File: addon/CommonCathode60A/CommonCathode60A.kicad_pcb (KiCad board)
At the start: 2 copper layers, 19 parts, among them J101 Conn_02x20_Odd_Even Header, J102 TBL008V-1000-08BE, J103 TBL008V-1000-08BE, K101 EW60-1A3-CL12D04, K102 EW60-1A3-CL12D04, K103 EW60-1A3-CL12D04, K104 EW60-1A3-CL12D04, K105 EW60-1A3-CL12D04, K106 EW60-1A3-CL12D04, K107 EW60-1A3-CL12D04, K108 EW60-1A3-CL12D04

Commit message: Better 60a board
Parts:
- moved H102 158.8 mm to (54.0, 133.0)
- moved H101 127.7 mm to (54.0, 27.0)
- moved J103 115.6 mm to (181.0, 125.0), turned to 90 degrees
- moved K101 90.3 mm to (154.0, 54.0), turned to 180 degrees
- moved K103 90.1 mm to (154.0, 74.0), turned to 180 degrees
- moved K107 82.9 mm to (154.0, 114.0), turned to 180 degrees
- moved K104 80.7 mm to (99.0, 74.0)
- moved K106 74.6 mm to (99.0, 94.0)
- moved H103 72.3 mm to (199.0, 27.0)
- moved J102 67.6 mm to (59.0, 125.0), turned to 90 degrees
- moved K102 67.3 mm to (99.0, 54.0)
- moved H104 50.2 mm to (199.0, 133.0)
- moved K108 34.5 mm to (99.0, 114.0)
- moved K105 28.4 mm to (154.0, 94.0), turned to 180 degrees
- moved J101 13.1 mm to (153.3, 40.1), turned to 270 degrees
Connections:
- net /K2_COIL_ON renamed /K4_COIL_ON
- J101 pad 13: /K2_COIL_OFF -> /K4_COIL_OFF
- J101 pad 14: /K2_COIL_OFF -> /K4_COIL_OFF
- K104 pad A2: /K2_COIL_OFF -> /K4_COIL_OFF
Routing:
- net /K3_OUT: track 0.00 -> 105.7 mm
- net /K1_OUT: track 0.00 -> 104.8 mm
- net /K2_OUT: track 0.00 -> 104.4 mm
- net /K4_OUT: track 0.00 -> 104.4 mm
- net /K8_IN: track 0.00 -> 103.0 mm
- net /K7_IN: track 0.00 -> 103.0 mm
- net /K6_IN: track 0.00 -> 103.0 mm
- net /K5_IN: track 0.00 -> 103.0 mm
- net /K5_OUT: track 0.00 -> 39.3 mm
- net /K8_OUT: track 0.00 -> 39.3 mm
- net /K7_OUT: track 0.00 -> 39.3 mm
- net /K6_OUT: track 0.00 -> 39.3 mm
- net /K1_IN: track 0.00 -> 36.9 mm
- net /K4_IN: track 0.00 -> 36.9 mm
- net /K3_IN: track 0.00 -> 36.9 mm
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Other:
- board outline added: 153 x 114 mm
- net class 30A Up to 230V AC added: clearance 1.25, trace_width 4, via_dia 9, via_drill 7
- net class 60A Up to 230V AC added: clearance 1.25, trace_width 8, via_dia 9, via_drill 7
- net class Default: clearance 0.2 -> 0.25; via_drill 0.4 -> 0.5
- rule trace_clearance: 0.2 -> 0.25

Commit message: Fix green
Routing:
- net /K5_OUT: track 39.3 -> 92.8 mm
- net /K8_OUT: track 39.3 -> 92.8 mm
- net /K7_OUT: track 39.3 -> 92.8 mm
- net /K6_OUT: track 39.3 -> 92.8 mm
- net /K4_IN: track 36.9 -> 88.7 mm
- net /K3_IN: track 36.9 -> 88.7 mm
- net /K2_IN: track 36.9 -> 88.7 mm
- net /K1_IN: track 36.9 -> 88.7 mm
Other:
- net class Default: clearance 0.25 -> 0.5; trace_width 0.25 -> 0.5
- rule trace_clearance: 0.25 -> 0.5

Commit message: Fix 60 Relay board
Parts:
- removed G101: LOGO_RUGLUDALLUR, BoatControl:Rugludallur-Logo_SilkScreen
- G102, LOGO102: moved to B.Cu
- LOGO101: footprint Symbol:KiCad-Logo2_20mm_SilkScreen -> Symbol:KiCad-Logo2_12mm_SilkScreen; moved to B.Cu
- moved LOGO101 391.9 mm to (73.0, 32.0)
- moved G102 324.8 mm to (125.5, 58.5)
- moved LOGO102 319.7 mm to (183.0, 33.5)
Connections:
- J101 pad 1: /K5_COIL_OFF -> /K1_COIL_ON
- J101 pad 10: /K6_COIL_OFF -> /K3_COIL_ON
- J101 pad 11: /K6_COIL_ON -> /K3_COIL_OFF
- J101 pad 12: /K6_COIL_ON -> /K3_COIL_OFF
- J101 pad 13: /K4_COIL_OFF -> /K4_COIL_ON
- J101 pad 14: /K4_COIL_OFF -> /K4_COIL_ON
- J101 pad 15: /K4_COIL_ON -> /K4_COIL_OFF
- J101 pad 16: /K4_COIL_ON -> /K4_COIL_OFF
- J101 pad 17: /K7_COIL_OFF -> /K5_COIL_ON
- J101 pad 18: /K7_COIL_OFF -> /K5_COIL_ON
- J101 pad 19: /K7_COIL_ON -> /K5_COIL_OFF
- J101 pad 2: /K5_COIL_OFF -> /K1_COIL_ON
- J101 pad 20: /K7_COIL_ON -> /K5_COIL_OFF
- J101 pad 21: /K3_COIL_OFF -> /K6_COIL_ON
- J101 pad 22: /K3_COIL_OFF -> /K6_COIL_ON
- J101 pad 23: /K3_COIL_ON -> /K6_COIL_OFF
- J101 pad 24: /K3_COIL_ON -> /K6_COIL_OFF
- J101 pad 25: /K8_COIL_OFF -> /K7_COIL_ON
- J101 pad 26: /K8_COIL_OFF -> /K7_COIL_ON
- J101 pad 27: /K8_COIL_ON -> /K7_COIL_OFF
- J101 pad 28: /K8_COIL_ON -> /K7_COIL_OFF
- J101 pad 29: /K4_COIL_OFF -> /K8_COIL_ON
- J101 pad 3: /K5_COIL_ON -> /K1_COIL_OFF
- J101 pad 30: /K4_COIL_OFF -> /K8_COIL_ON
- J101 pad 31: /K8_COIL_ON -> /K8_COIL_OFF
- J101 pad 32: /K8_COIL_ON -> /K8_COIL_OFF
- J101 pad 4: /K5_COIL_ON -> /K1_COIL_OFF
- J101 pad 5: /K2_COIL_OFF -> /K2_COIL_ON
- J101 pad 6: /K2_COIL_OFF -> /K2_COIL_ON
- J101 pad 7: /K1_COIL_ON -> /K2_COIL_OFF
- J101 pad 8: /K1_COIL_ON -> /K2_COIL_OFF
- J101 pad 9: /K6_COIL_OFF -> /K3_COIL_ON
- J102 pad 1_1: /K4_IN -> /K8_IN
- J102 pad 1_2: /K4_IN -> /K8_IN
- J102 pad 1_3: /K4_IN -> /K8_IN
- J102 pad 2_1: /K8_IN -> /K7_IN
- J102 pad 2_2: /K8_IN -> /K7_IN
- J102 pad 2_3: /K8_IN -> /K7_IN
- J102 pad 3_1: /K3_IN -> /K6_IN
- J102 pad 3_2: /K3_IN -> /K6_IN
- J102 pad 3_3: /K3_IN -> /K6_IN
- J102 pad 4_1: /K7_IN -> /K5_IN
- J102 pad 4_2: /K7_IN -> /K5_IN
- J102 pad 4_3: /K7_IN -> /K5_IN
- J102 pad 5_1: /K2_IN -> /K4_IN
- J102 pad 5_2: /K2_IN -> /K4_IN
- J102 pad 5_3: /K2_IN -> /K4_IN
- J102 pad 6_1: /K6_IN -> /K3_IN
- J102 pad 6_2: /K6_IN -> /K3_IN
- J102 pad 6_3: /K6_IN -> /K3_IN
- J102 pad 7_1: /K1_IN -> /K2_IN
- J102 pad 7_2: /K1_IN -> /K2_IN
- J102 pad 7_3: /K1_IN -> /K2_IN
- J102 pad 8_1: /K5_IN -> /K1_IN
- J102 pad 8_2: /K5_IN -> /K1_IN
- J102 pad 8_3: /K5_IN -> /K1_IN
- J103 pad 1_1: /K4_OUT -> /K8_OUT
- J103 pad 1_2: /K4_OUT -> /K8_OUT
- J103 pad 1_3: /K4_OUT -> /K8_OUT
- J103 pad 2_1: /K8_OUT -> /K7_OUT
- J103 pad 2_2: /K8_OUT -> /K7_OUT
- J103 pad 2_3: /K8_OUT -> /K7_OUT
- J103 pad 3_1: /K3_OUT -> /K6_OUT
- J103 pad 3_2: /K3_OUT -> /K6_OUT
- J103 pad 3_3: /K3_OUT -> /K6_OUT
- J103 pad 4_1: /K7_OUT -> /K5_OUT
- J103 pad 4_2: /K7_OUT -> /K5_OUT
- J103 pad 4_3: /K7_OUT -> /K5_OUT
- J103 pad 5_1: /K2_OUT -> /K4_OUT
- J103 pad 5_2: /K2_OUT -> /K4_OUT
- J103 pad 5_3: /K2_OUT -> /K4_OUT
- J103 pad 6_1: /K6_OUT -> /K3_OUT
- J103 pad 6_2: /K6_OUT -> /K3_OUT
- J103 pad 6_3: /K6_OUT -> /K3_OUT
- J103 pad 7_1: /K1_OUT -> /K2_OUT
- J103 pad 7_2: /K1_OUT -> /K2_OUT
- J103 pad 7_3: /K1_OUT -> /K2_OUT
- J103 pad 8_1: /K5_OUT -> /K1_OUT
- J103 pad 8_2: /K5_OUT -> /K1_OUT
- J103 pad 8_3: /K5_OUT -> /K1_OUT
- K101 pad 1: /K5_OUT -> /K1_OUT
- K101 pad 2: /K5_OUT -> /K1_OUT
- K101 pad 3: /K5_OUT -> /K1_OUT
- K101 pad 4: /K5_IN -> /K1_IN
- K101 pad 5: /K5_IN -> /K1_IN
- K101 pad 6: /K5_IN -> /K1_IN
- K101 pad A2: /K5_COIL_ON -> /K1_COIL_OFF
- K101 pad A3: /K5_COIL_OFF -> /K1_COIL_ON
- K102 pad 1: /K1_IN -> /K2_IN
- K102 pad 2: /K1_IN -> /K2_IN
- K102 pad 3: /K1_IN -> /K2_IN
- K102 pad 4: /K1_OUT -> /K2_OUT
- K102 pad 5: /K1_OUT -> /K2_OUT
- K102 pad 6: /K1_OUT -> /K2_OUT
- K102 pad A2: /K2_COIL_OFF -> /K2_COIL_ON
- K102 pad A3: /K1_COIL_ON -> /K2_COIL_OFF
- K103 pad 1: /K6_OUT -> /K3_OUT
- K103 pad 2: /K6_OUT -> /K3_OUT
- K103 pad 3: /K6_OUT -> /K3_OUT
- K103 pad 4: /K6_IN -> /K3_IN
- K103 pad 5: /K6_IN -> /K3_IN
- K103 pad 6: /K6_IN -> /K3_IN
- K103 pad A2: /K6_COIL_ON -> /K3_COIL_OFF
- K103 pad A3: /K6_COIL_OFF -> /K3_COIL_ON
- K104 pad 1: /K2_IN -> /K4_IN
- K104 pad 2: /K2_IN -> /K4_IN
- K104 pad 3: /K2_IN -> /K4_IN
- K104 pad 4: /K2_OUT -> /K4_OUT
- K104 pad 5: /K2_OUT -> /K4_OUT
- K104 pad 6: /K2_OUT -> /K4_OUT
- K104 pad A2: /K4_COIL_OFF -> /K4_COIL_ON
- K104 pad A3: /K4_COIL_ON -> /K4_COIL_OFF
- K105 pad 1: /K7_OUT -> /K5_OUT
- K105 pad 2: /K7_OUT -> /K5_OUT
- K105 pad 3: /K7_OUT -> /K5_OUT
- K105 pad 4: /K7_IN -> /K5_IN
- K105 pad 5: /K7_IN -> /K5_IN
- K105 pad 6: /K7_IN -> /K5_IN
- K105 pad A2: /K7_COIL_ON -> /K5_COIL_OFF
- K105 pad A3: /K7_COIL_OFF -> /K5_COIL_ON
- K106 pad 1: /K3_IN -> /K6_IN
- K106 pad 2: /K3_IN -> /K6_IN
- K106 pad 3: /K3_IN -> /K6_IN
- K106 pad 4: /K3_OUT -> /K6_OUT
- K106 pad 5: /K3_OUT -> /K6_OUT
- K106 pad 6: /K3_OUT -> /K6_OUT
- K106 pad A2: /K3_COIL_OFF -> /K6_COIL_ON
- K106 pad A3: /K3_COIL_ON -> /K6_COIL_OFF
- K107 pad 1: /K8_OUT -> /K7_OUT
- K107 pad 2: /K8_OUT -> /K7_OUT
- K107 pad 3: /K8_OUT -> /K7_OUT
- K107 pad 4: /K8_IN -> /K7_IN
- K107 pad 5: /K8_IN -> /K7_IN
- K107 pad 6: /K8_IN -> /K7_IN
- K107 pad A2: /K8_COIL_ON -> /K7_COIL_OFF
- K107 pad A3: /K8_COIL_OFF -> /K7_COIL_ON
- K108 pad 1: /K4_IN -> /K8_IN
- K108 pad 2: /K4_IN -> /K8_IN
- K108 pad 3: /K4_IN -> /K8_IN
- K108 pad 4: /K4_OUT -> /K8_OUT
- K108 pad 5: /K4_OUT -> /K8_OUT
- K108 pad 6: /K4_OUT -> /K8_OUT
- K108 pad A2: /K4_COIL_OFF -> /K8_COIL_ON
- K108 pad A3: /K8_COIL_ON -> /K8_COIL_OFF
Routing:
- net GND: track 0.00 -> 205.5 mm
- net /K4_COIL_ON: track 0.00 -> 105.0 mm
- net /K2_COIL_OFF: track 0.00 -> 93.5 mm
- net /K8_COIL_OFF: track 0.00 -> 90.8 mm
- net /K8_COIL_ON: track 0.00 -> 86.9 mm
- net /K4_COIL_OFF: track 0.00 -> 85.0 mm
- net /K2_COIL_ON: track 0.00 -> 84.2 mm
- net /K7_COIL_ON: track 0.00 -> 83.7 mm
- net /K7_COIL_OFF: track 0.00 -> 80.5 mm
- net /K6_COIL_OFF: track 0.00 -> 74.2 mm
- net /K6_COIL_ON: track 0.00 -> 71.1 mm
- net /K5_COIL_ON: track 0.00 -> 59.4 mm
- net /K5_COIL_OFF: track 0.00 -> 56.3 mm
- net /K6_IN: track 103.0 -> 51.1 mm
- net /K3_COIL_OFF: track 0.00 -> 37.1 mm
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- added copper zone on In1.Cu, net GND
- added copper zone on In2.Cu, net GND
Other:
- copper layers 2 -> 4
- net class Default: clearance 0.5 -> 0.6; trace_width 0.5 -> 1
- rule trace_clearance: 0.5 -> 0.6
- rule trace_min: 0.2 -> 0.5
- board text added: "13oz B.Cu"
- board text added: "13oz F.Cu"
- board text added: "1oz In1.Cu"
- board text added: "1oz In2.Cu"
- board text added: "4 Layers (13oz -1oz - 1oz - 13oz)"
- board text added: "Board Details"
- board text added: "Core"
- board text added: "Dimentions 153m x 114mm (+/- 0.15mm)"
- board text added: "HASL"
- board text added: "Minimum Character Width(Legend) 0.15mm"
- board text added: "Minimum F/B trace width/spacing 1.25mm"
- board text added: "Minimum In1/In2 trace width/spacing 0.6mm"
- board text added: "Prepreg"
- board text added: "Soldermask"
- board text added: "Stack-Up"
- board text added: "Thickness 1.6 - 3.2mm (+/-10%) (routed)"
- board text added: "bc@ant.st"
- board text added: "https://github.com/antevens/boatcontrol"

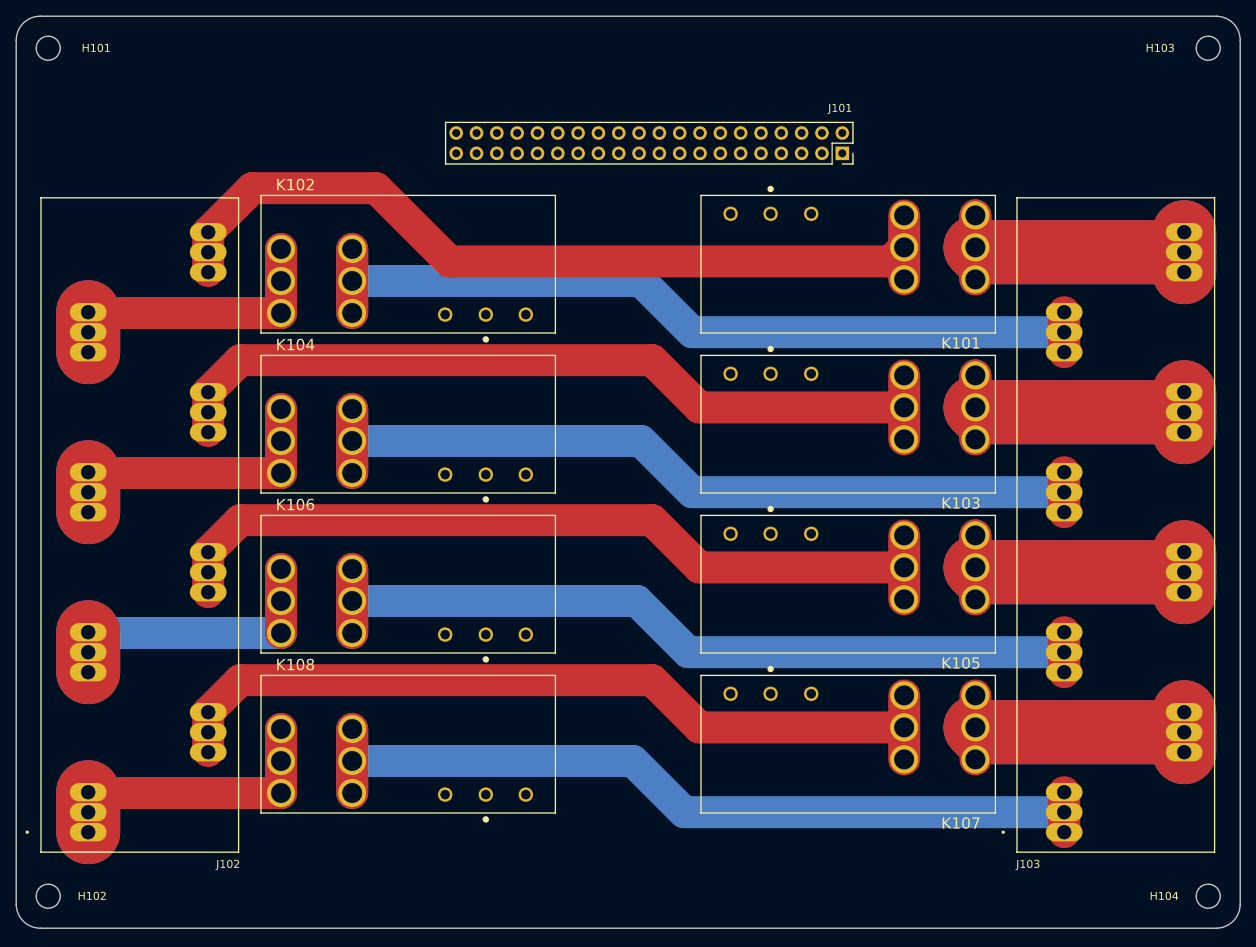
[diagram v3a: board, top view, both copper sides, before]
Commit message: Final for 60A Addon Board
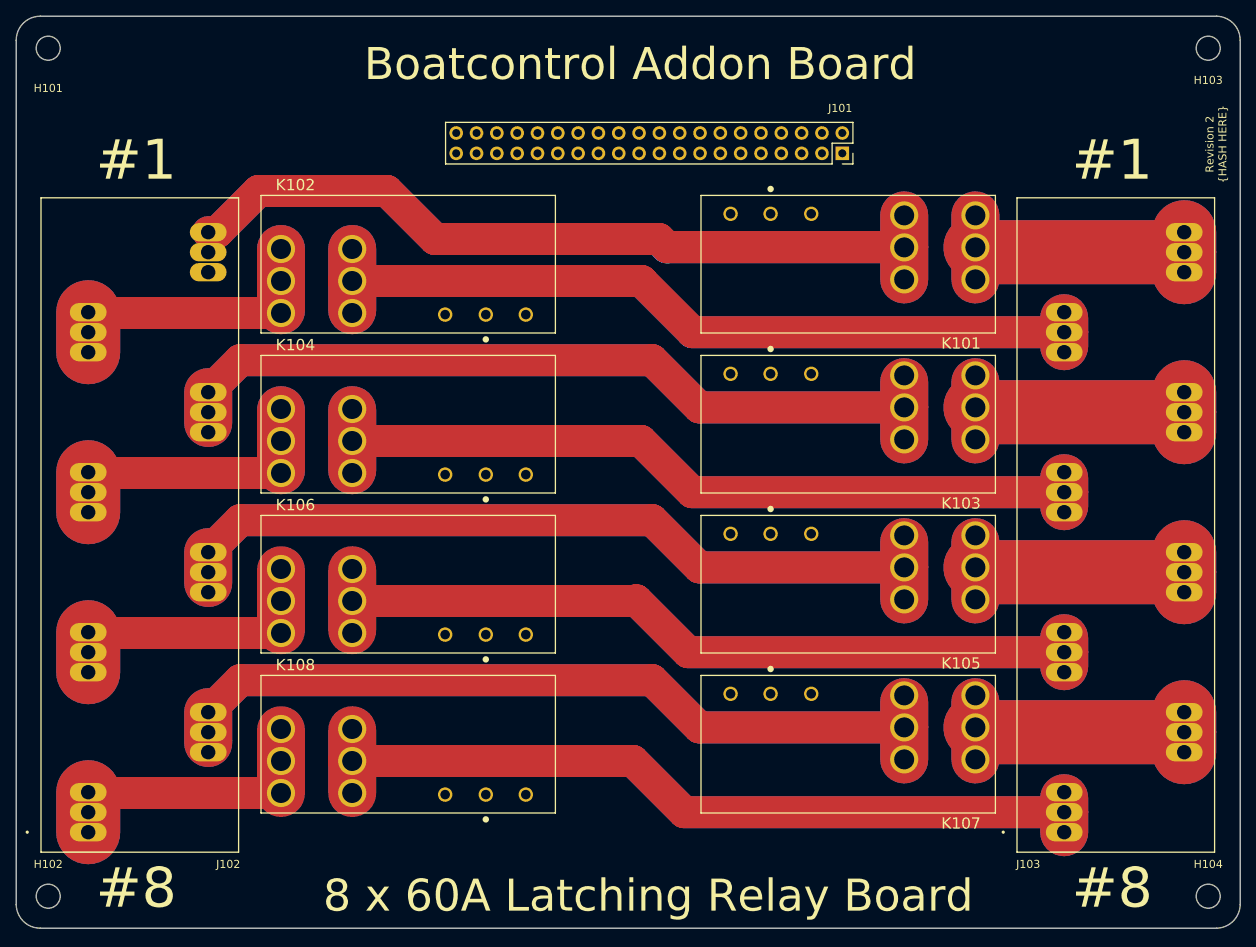
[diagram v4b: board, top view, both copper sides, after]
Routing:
- net /K4_OUT: track 112.7 -> 213.3 mm
- net /K7_IN: track 104.0 -> 204.2 mm
- net /K3_IN: track 104.0 -> 204.2 mm
- net /K5_IN: track 104.1 -> 204.2 mm
- net /K8_OUT: track 112.7 -> 207.7 mm
- net /K1_IN: track 106.6 -> 200.1 mm
- net /K6_OUT: track 112.7 -> 205.9 mm
- net /K2_OUT: track 112.7 -> 205.6 mm
- net /K6_IN: track 51.1 -> 74.7 mm
- net /K1_OUT: track 78.7 -> 86.7 mm
- net /K4_IN: track 76.2 -> 83.2 mm
- net /K7_OUT: track 70.7 -> 77.0 mm
- net /K5_OUT: track 78.7 -> 85.0 mm
- net /K3_OUT: track 78.7 -> 85.0 mm
- net /K2_IN: track 76.2 -> 75.5 mm
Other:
- board text added: "#1"
- board text added: "#8"
- board text added: "8 x 60A Latching Relay Board"
- board text added: "Boatcontrol Addon Board"
- board text added: "Revision 2 {HASH HERE}"

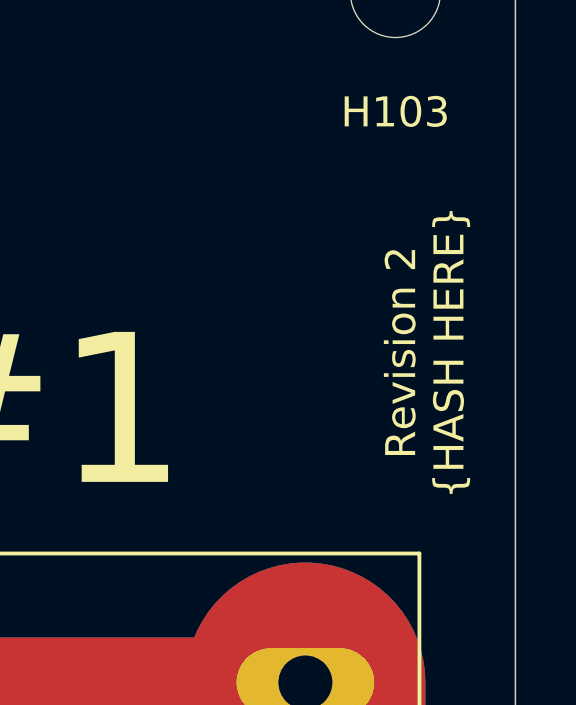
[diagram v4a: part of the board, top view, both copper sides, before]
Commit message: Add git refs for 60A addon board
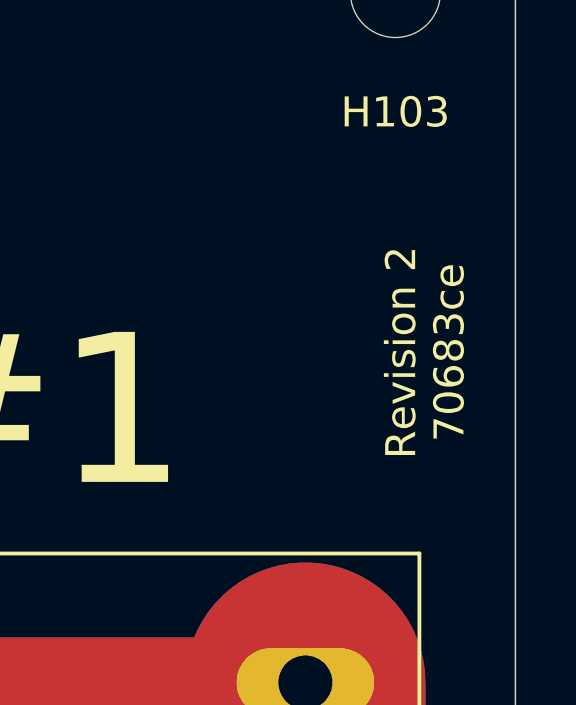
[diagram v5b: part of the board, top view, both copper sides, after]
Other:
- board text added: "Revision 2 70683ce"
- board text removed: "Revision 2 {HASH HERE}"
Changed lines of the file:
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@@
   )
   (page A4)
+  (title_block
+    (title BoatControl)
+    (date 2021-04-09)
+    (rev 2)
+    (company Rugludallur)
+    (comment 1 "8x 60A Latching Relay Addon board for Boatcontrol")
+    (comment 2 https://github.com/antevens/boatcontrol/addon/CommonCathode60A)
+    (comment 3 a@ant.st)
+    (comment 4 70683ce0ebce79e47096088a795a31fc68ff9315)
+  )
   (layers
     (0 F.Cu power)
@@
     (arrow2b (pts (xy 205 133) (xy 204.413579 131.873496)))
   )
-  (gr_text "Revision 2\n{HASH HERE}" (at 200 39 90) (layer F.SilkS)
+  (gr_text "Revision 2\n70683ce" (at 200 39 90) (layer F.SilkS)
     (effects (font (size 1 1) (thickness 0.15)))
   )
